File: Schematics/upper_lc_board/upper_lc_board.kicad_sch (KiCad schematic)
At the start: 0 parts

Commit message: more organizational work, add shared footprint, model, symbol dirs and clean up individuals
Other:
- title: Upper Launch Control Board -> PHEONIX | Upper Control Board
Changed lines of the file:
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@@
 	(paper "A4")
 	(title_block
-		(title "Upper Launch Control Board")
+		(title "PHEONIX | Upper Control Board")
 		(rev "A")
 		(company "Queen's Rocket Engineering Team")
+		(comment 1 "Jeevan Sanchez")
 	)
 	(sheet

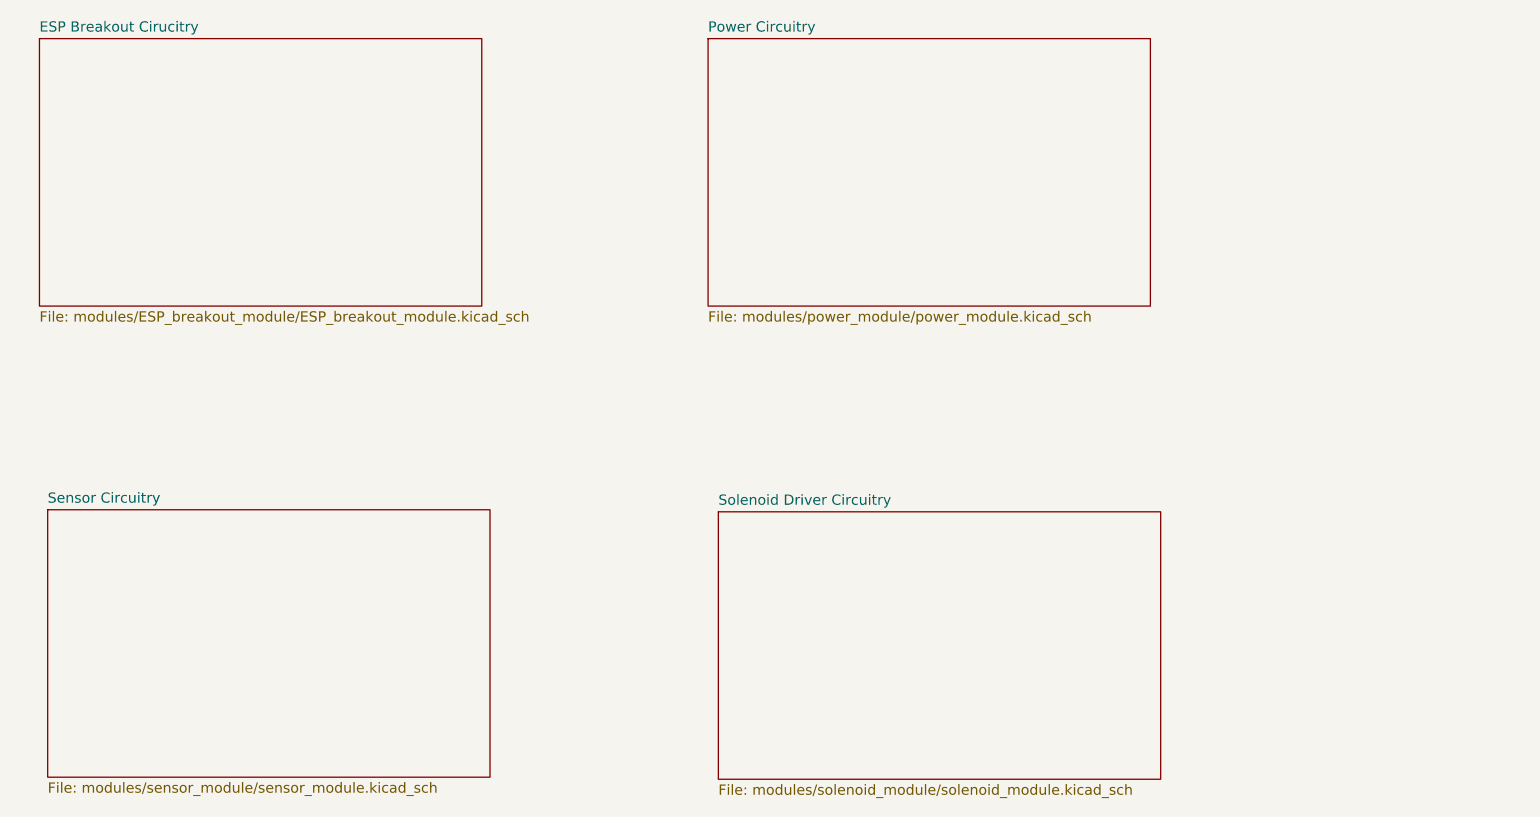
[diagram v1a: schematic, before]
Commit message: move lc v2 to og folder
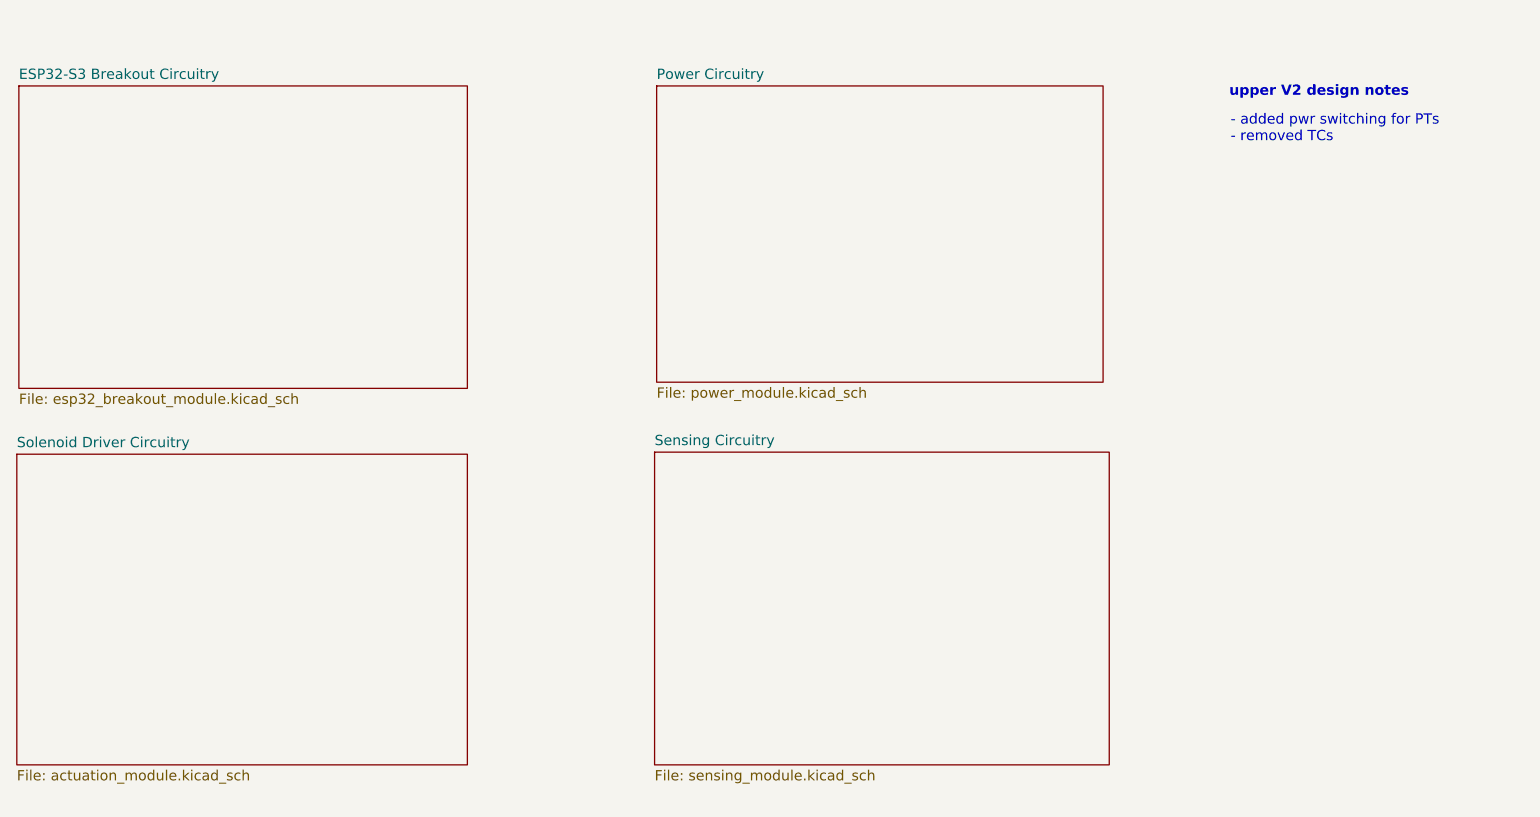
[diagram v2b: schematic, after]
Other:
- removed sheet ESP Breakout Cirucitry
- removed sheet Sensor Circuitry
- added sheet ESP32-S3 Breakout Circuitry (esp32_breakout_module.kicad_sch)
- added sheet Sensing Circuitry (sensing_module.kicad_sch)
- sheet Power Circuitry: file modules/power_module/power_module.kicad_sch -> power_module.kicad_sch
- sheet Solenoid Driver Circuitry: file modules/solenoid_module/solenoid_module.kicad_sch -> actuation_module.kicad_sch
- note added: "- added pwr switching for PTs - removed TCs"
- note added: "upper V2 design notes"
- title: PHEONIX | Upper Control Board -> Pegasus
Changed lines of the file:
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@@
 	(paper "A4")
 	(title_block
-		(title "PHEONIX | Upper Control Board")
-		(rev "A")
+		(title "Pegasus")
 		(company "Queen's Rocket Engineering Team")
-		(comment 1 "Jeevan Sanchez")
+		(comment 1 "Upper Control Board V2")
+		(comment 2 "Jeevan Sanchez")
+	)
+	(text "- added pwr switching for PTs\n- removed TCs "
+		(exclude_from_sim no)
+		(at 218.186 55.626 0)
+		(effects
+			(font
+				(size 1.27 1.27)
+				(color 0 0 0 1)
+			)
+			(justify left)
+		)
+	)
+	(text "upper V2 design notes"
+		(exclude_from_sim no)
+		(at 229.108 51.054 0)
+		(effects
+			(font
+				(size 1.27 1.27)
+				(thickness 0.254)
+				(bold yes)
+				(color 0 0 0 1)
+			)
+		)
 	)
 	(sheet
-		(at 72.136 102.616)
-		(size 54.61 33.02)
+		(at 147.066 95.504)
+		(size 56.134 38.608)
 		(fields_autoplaced yes)
 		(stroke
@@
 			(color 0 0 0 0.0000)
 		)
-		(property "Sheetname" "Sensor Circuitry"
-			(at 72.136 101.9044 0)
+		(property "Sheetname" "Sensing Circuitry"
+			(at 147.066 94.7924 0)
 			(effects
 				(font
@@
 			)
 		)
-		(property "Sheetfile" "modules/sensor_module/sensor_module.kicad_sch"
-			(at 72.136 136.2206 0)
+		(property "Sheetfile" "sensing_module.kicad_sch"
+			(at 147.066 134.6966 0)
 			(effects
 				(font
@@
 		)
 		(instances
-			(project "upper_lc_board"
-				(path "/9b1a1d2a-fad7-4f10-83f3-1f83e9656c75"
-					(page "4")
+			(project "upper_lc_board_v2"
+				(path "/8de962ac-ee95-4233-a205-efbcd04063bc"
+					(page "5")
 				)
 			)
@@
 	)
 	(sheet
-		(at 71.12 44.45)
-		(size 54.61 33.02)
-		(fields_autoplaced yes)
-		(stroke
-			(width 0.1524)
-			(type solid)
-		)
-		(fill
-			(color 0 0 0 0.0000)
-		)
-		(property "Sheetname" "ESP Breakout Cirucitry"
-			(at 71.12 43.7384 0)
-			(effects
-				(font
-					(size 1.27 1.27)
-				)
-				(justify left bottom)
-			)
-		)
-		(property "Sheetfile" "modules/ESP_breakout_module/ESP_breakout_module.kicad_sch"
-			(at 71.12 78.0546 0)
-			(effects
-				(font
-					(size 1.27 1.27)
-				)
-				(justify left top)
-			)
-		)
-		(instances
-			(project "upper_lc_board"
-				(path "/9b1a1d2a-fad7-4f10-83f3-1f83e9656c75"
-					(page "2")
-				)
-			)
-		)
-	)
-	(sheet
-		(at 153.67 44.45)
-		(size 54.61 33.02)
+		(at 147.32 50.292)
+		(size 55.118 36.576)
 		(fields_autoplaced yes)
 		(stroke
@@
 		)
 		(property "Sheetname" "Power Circuitry"
-			(at 153.67 43.7384 0)
+			(at 147.32 49.5804 0)
 			(effects
 				(font
@@
 			)
 		)
-		(property "Sheetfile" "modules/power_module/power_module.kicad_sch"
-			(at 153.67 78.0546 0)
+		(property "Sheetfile" "power_module.kicad_sch"
+			(at 147.32 87.4526 0)
 			(effects
 				(font
@@
 		)
 		(instances
-			(project "upper_lc_board"
-				(path "/9b1a1d2a-fad7-4f10-83f3-1f83e9656c75"
+			(project "upper_lc_board_v2"
+				(path "/8de962ac-ee95-4233-a205-efbcd04063bc"
 					(page "3")
 				)
@@
 	)
 	(sheet
-		(at 154.94 102.87)
-		(size 54.61 33.02)
+		(at 68.326 95.758)
+		(size 55.626 38.354)
 		(fields_autoplaced yes)
 		(stroke
@@
 		)
 		(property "Sheetname" "Solenoid Driver Circuitry"
-			(at 154.94 102.1584 0)
+			(at 68.326 95.0464 0)
 			(effects
 				(font
@@
 			)
 		)
-		(property "Sheetfile" "modules/solenoid_module/solenoid_module.kicad_sch"
-			(at 154.94 136.4746 0)
+		(property "Sheetfile" "actuation_module.kicad_sch"
+			(at 68.326 134.6966 0)
 			(effects
 				(font
@@
 		)
 		(instances
-			(project "upper_lc_board"
-				(path "/9b1a1d2a-fad7-4f10-83f3-1f83e9656c75"
-					(page "5")
+			(project "upper_lc_board_v2"
+				(path "/8de962ac-ee95-4233-a205-efbcd04063bc"
+					(page "4")
 				)
 			)
+		)
+	)
+	(sheet
+		(at 68.58 50.292)
+		(size 55.372 37.338)
+		(fields_autoplaced yes)
+		(stroke
+			(width 0.1524)
+			(type solid)
+		)
+		(fill
+			(color 0 0 0 0.0000)
+		)
+		(property "Sheetname" "ESP32-S3 Breakout Circuitry"
+			(at 68.58 49.5804 0)
+			(effects
+				(font
+					(size 1.27 1.27)
+				)
+				(justify left bottom)
+			)
+		)
+		(property "Sheetfile" "esp32_breakout_module.kicad_sch"
+			(at 68.58 88.2146 0)
+			(effects
+				(font
+					(size 1.27 1.27)
+				)
+				(justify left top)
+			)
+		)
+		(instances
+			(project "upper_lc_board_v2"
+				(path "/8de962ac-ee95-4233-a205-efbcd04063bc"
+					(page "2")
+				)
+			)

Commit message: add board-specifc READMEs (TODO), cleanup schematic titles
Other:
- title: Pegasus -> QRET 25-26 SRAD Hybrid Upper Control Module
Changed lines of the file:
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@@
 	(paper "A4")
 	(title_block
-		(title "Pegasus")
+		(title "QRET 25-26 SRAD Hybrid Upper Control Module")
 		(company "Queen's Rocket Engineering Team")
 		(comment 1 "Upper Control Board V2")
-		(comment 2 "Jeevan Sanchez")
+		(comment 2 "Jeevan Sanchez, Tristan Alderson")
 	)
 	(text "- added pwr switching for PTs\n- removed TCs "
